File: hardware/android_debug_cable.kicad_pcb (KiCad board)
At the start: 2 copper layers, 36.7 x 12.2 mm, 12 parts, among them P1 USB_A, P2 CONN_01X04, P3 SJ-43514-SMT-TR, U1 TPS71718DCKR, U2 CP2103-GM

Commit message: Remove Copperhead branding, bump to v0.3
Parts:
- removed W1: LOGO, copperhead_logo:copperhead_logo
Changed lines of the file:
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@@
-(kicad_pcb (version 20160815) (host pcbnew 201610010949+7276~55~ubuntu16.04.1-)
+(kicad_pcb (version 20160815) (host pcbnew no-vcs-found-7409~56~ubuntu16.10.1)
   (general
     (links 33)
@@
     (tracks 205)
     (zones 0)
-    (modules 12)
+    (modules 11)
     (nets 10)
   )
@@
       (effects (font (size 0.7 0.7) (thickness 0.15)))
     )
-    (fp_text value SJ-43514-SMT-TR (at 3.8735 7.874 360) (layer F.Fab)
+    (fp_text value SJ-43514-SMT-TR (at 3.8735 7.874) (layer F.Fab)
       (effects (font (size 1 1) (thickness 0.15)))
     )
@@
     )
   )
-  (module copperhead_logo:copperhead_logo (layer B.Cu)
-    (at 94.2 82.1)
-    (fp_text reference W1 (at 0 0) (layer B.SilkS) hide
-      (effects (font (thickness 0.3)) (justify mirror))
-    )
-    (fp_text value LOGO (at 0.75 0) (layer B.SilkS) hide
-      (effects (font (thickness 0.3)) (justify mirror))
-    )
-    (fp_poly (pts (xy 0.286595 4.997953) (xy 0.652425 4.97361) (xy 0.978773 4.925874) (xy 1.513452 4.793043)
-      (xy 2.009899 4.611833) (xy 2.473986 4.379106) (xy 2.911581 4.091724) (xy 3.328554 3.746551)
-      (xy 3.50953 3.573031) (xy 3.882533 3.161764) (xy 4.196417 2.731413) (xy 4.45407 2.276573)
-      (xy 4.658382 1.791838) (xy 4.812242 1.271805) (xy 4.862373 1.042274) (xy 4.910585 0.711301)
-      (xy 4.934611 0.345163) (xy 4.934452 -0.032595) (xy 4.910109 -0.398425) (xy 4.862373 -0.724773)
-      (xy 4.728781 -1.261192) (xy 4.545946 -1.760049) (xy 4.31098 -2.226749) (xy 4.020993 -2.666697)
-      (xy 3.673096 -3.085297) (xy 3.50953 -3.25553) (xy 3.095062 -3.631) (xy 2.660805 -3.947073)
-      (xy 2.202899 -4.205819) (xy 1.717484 -4.409311) (xy 1.200701 -4.559619) (xy 1.000125 -4.602293)
-      (xy 0.77577 -4.637061) (xy 0.517751 -4.663239) (xy 0.246379 -4.679854) (xy -0.018034 -4.685937)
-      (xy -0.255177 -4.680517) (xy -0.396875 -4.669035) (xy -0.95683 -4.57297) (xy -1.492599 -4.418811)
-      (xy -2.001529 -4.208039) (xy -2.480971 -3.942137) (xy -2.928275 -3.622585) (xy -3.340789 -3.250867)
-      (xy -3.715863 -2.828462) (xy -3.736754 -2.802004) (xy -4.045523 -2.358026) (xy -4.29936 -1.886324)
-      (xy -4.497617 -1.392117) (xy -4.639646 -0.880626) (xy -4.724799 -0.357072) (xy -4.75243 0.173326)
-      (xy -4.722283 0.6985) (xy -2.604785 0.6985) (xy -2.51683 0.545361) (xy -2.30908 0.183999)
-      (xy -2.100804 -0.177609) (xy -1.894435 -0.535281) (xy -1.692406 -0.884836) (xy -1.497151 -1.222092)
-      (xy -1.311103 -1.542868) (xy -1.136697 -1.84298) (xy -0.976364 -2.118249) (xy -0.832538 -2.364491)
-      (xy -0.707654 -2.577526) (xy -0.604144 -2.753172) (xy -0.524441 -2.887246) (xy -0.47098 -2.975568)
-      (xy -0.446194 -3.013955) (xy -0.444822 -3.015284) (xy -0.426146 -2.988446) (xy -0.379172 -2.912028)
-      (xy -0.307152 -2.791559) (xy -0.213336 -2.632567) (xy -0.100976 -2.440581) (xy 0.026679 -2.221131)
-      (xy 0.166376 -1.979743) (xy 0.278627 -1.784971) (xy 0.442484 -1.500212) (xy 0.610981 -1.207497)
-      (xy 0.778367 -0.916808) (xy 0.93889 -0.63813) (xy 1.086799 -0.381446) (xy 1.216344 -0.15674)
-      (xy 1.321774 0.026006) (xy 1.348733 0.072699) (xy 1.711587 0.701022) (xy 1.454789 0.691824)
-      (xy 1.197992 0.682625) (xy 0.386323 -0.722312) (xy 0.228568 -0.994639) (xy 0.080067 -1.249569)
-      (xy -0.056115 -1.48194) (xy -0.176914 -1.686592) (xy -0.279267 -1.858364) (xy -0.36011 -1.992097)
-      (xy -0.416379 -2.082629) (xy -0.445011 -2.1248) (xy -0.447752 -2.12725) (xy -0.46749 -2.100571)
-      (xy -0.515783 -2.023965) (xy -0.589579 -1.902579) (xy -0.685822 -1.74156) (xy -0.80146 -1.546054)
-      (xy -0.933438 -1.321209) (xy -1.078703 -1.072172) (xy -1.234201 -0.804088) (xy -1.286053 -0.714375)
-      (xy -2.101947 0.6985) (xy -2.604785 0.6985) (xy -4.722283 0.6985) (xy -4.72189 0.705345)
-      (xy -4.632532 1.233766) (xy -4.483708 1.753369) (xy -4.345514 2.105153) (xy -4.127076 2.54)
-      (xy -2.597748 2.54) (xy -1.529062 0.6855) (xy -1.30419 0.296075) (xy -1.108823 -0.040466)
-      (xy -0.94143 -0.326643) (xy -0.800483 -0.564974) (xy -0.684453 -0.757975) (xy -0.59181 -0.908165)
-      (xy -0.521027 -1.018062) (xy -0.470574 -1.090183) (xy -0.438921 -1.127047) (xy -0.425271 -1.132188)
-      (xy -0.391849 -1.086032) (xy -0.340594 -1.003433) (xy -0.293013 -0.92075) (xy -0.19586 -0.746125)
-      (xy -1.01868 0.677698) (xy -1.177131 0.95212) (xy -1.325549 1.209622) (xy -1.460973 1.445034)
-      (xy -1.554371 1.607766) (xy -0.974568 1.607766) (xy -0.965463 1.57683) (xy -0.930335 1.506465)
-      (xy -0.876531 1.411264) (xy -0.870541 1.401166) (xy -0.754579 1.2065) (xy 0.896107 1.2065)
-      (xy 1.262239 1.206405) (xy 1.569856 1.206007) (xy 1.823946 1.205134) (xy 2.029492 1.203618)
-      (xy 2.191481 1.201289) (xy 2.3149 1.197976) (xy 2.404732 1.19351) (xy 2.465965 1.18772)
-      (xy 2.503583 1.180437) (xy 2.522573 1.17149) (xy 2.527921 1.16071) (xy 2.525835 1.150938)
-      (xy 2.506213 1.113162) (xy 2.457891 1.025927) (xy 2.383998 0.894724) (xy 2.28766 0.725043)
-      (xy 2.172005 0.522374) (xy 2.04016 0.292208) (xy 1.895252 0.040035) (xy 1.740408 -0.228655)
-      (xy 1.712813 -0.27646) (xy 1.557397 -0.546069) (xy 1.412076 -0.798995) (xy 1.279873 -1.029923)
-      (xy 1.163808 -1.233536) (xy 1.066903 -1.404515) (xy 0.992178 -1.537546) (xy 0.942656 -1.627309)
-      (xy 0.921357 -1.668489) (xy 0.92075 -1.670409) (xy 0.935226 -1.712536) (xy 0.972357 -1.786109)
-      (xy 1.022697 -1.875322) (xy 1.076798 -1.964366) (xy 1.125213 -2.037434) (xy 1.158496 -2.078718)
-      (xy 1.166855 -2.082227) (xy 1.185409 -2.052333) (xy 1.23301 -1.97199) (xy 1.307 -1.845768)
-      (xy 1.404723 -1.678237) (xy 1.523522 -1.473969) (xy 1.66074 -1.237534) (xy 1.813721 -0.973501)
-      (xy 1.979808 -0.686443) (xy 2.156345 -0.380929) (xy 2.24325 -0.230393) (xy 3.301579 1.603375)
-      (xy 1.169473 1.611538) (xy 0.80752 1.61275) (xy 0.464566 1.613561) (xy 0.145837 1.613981)
-      (xy -0.143443 1.614018) (xy -0.398046 1.613682) (xy -0.612748 1.612982) (xy -0.782322 1.611927)
-      (xy -0.901542 1.610527) (xy -0.965183 1.60879) (xy -0.974568 1.607766) (xy -1.554371 1.607766)
-      (xy -1.58044 1.653186) (xy -1.680989 1.828906) (xy -1.759658 1.967026) (xy -1.813485 2.062373)
-      (xy -1.839508 2.109778) (xy -1.8415 2.114102) (xy -1.810731 2.116667) (xy -1.722347 2.119366)
-      (xy -1.582232 2.122126) (xy -1.396271 2.124871) (xy -1.170348 2.127529) (xy -0.910348 2.130026)
-      (xy -0.622155 2.132287) (xy -0.311654 2.134239) (xy -0.184798 2.134905) (xy 1.471905 2.143125)
-      (xy 1.576091 2.31775) (xy 1.630232 2.41166) (xy 1.668352 2.483805) (xy 1.681513 2.516188)
-      (xy 1.65084 2.520218) (xy 1.561839 2.524034) (xy 1.419685 2.527578) (xy 1.229552 2.530792)
-      (xy 0.996611 2.533618) (xy 0.726038 2.536) (xy 0.423004 2.537879) (xy 0.092683 2.539198)
-      (xy -0.259752 2.539899) (xy -0.457499 2.54) (xy -2.597748 2.54) (xy -4.127076 2.54)
-      (xy -4.125196 2.543742) (xy -3.859523 2.954886) (xy -3.541054 3.349523) (xy -3.383147 3.519858)
-      (xy -2.974596 3.900625) (xy -2.535891 4.225754) (xy -2.065994 4.495807) (xy -1.563866 4.711348)
-      (xy -1.02847 4.872938) (xy -0.788274 4.925874) (xy -0.457301 4.974086) (xy -0.091163 4.998112)
-      (xy 0.286595 4.997953)) (layer B.SilkS) (width 0.01))
-  )
   (module Resistors_SMD:R_0402 (layer F.Cu)

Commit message: Add first version of v0.4
Signed-off-by: Robert Foss <robert.foss@collabora.com>
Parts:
- removed C5: 1uF, Capacitors_SMD:C_0402
- removed C6: 0.1uF, Capacitors_SMD:C_0402
- added C3: 1uF, Capacitors_SMD:C_0402, F.Cu at (138.8, 91.7)
- added G***: LOGO, memcpy_logo:memcpy_logo_13.2x3.6mm, B.Cu at (139.6, 88.8)
- C1: value 0.1uF -> 1uF
- P1: value USB_A -> USB_OTG; footprint connectors:usb-PCB -> Connectors:USB_Micro-B
- P2: value CONN_01X04 -> 50-00397; footprint footprints:CONN_2.54mm_1x4_no-outline -> 50-00397:50-00397
- P3: value SJ-43514-SMT-TR -> CONN_01X04; footprint 3-5mm_4pole_jack:3.5mm_4pin_jack -> footprints:CONN_2.54mm_1x4_no-outline
- R1: value 10k -> 1k
- U1: value TPS71718DCKR -> TCR2EF18; footprint TO_SOT_Packages_SMD:SC-70-5 -> TO_SOT_Packages_SMD:SOT-23-5
- U2: value CP2103-GM -> CP2102N-A01-GQFN24; footprint Housings_DFN_QFN:QFN-28-1EP_5x5mm_Pitch0.5mm -> Housings_DFN_QFN:QFN-24-1EP_4x4mm_Pitch0.5mm
- moved P1 57.3 mm to (135.2, 88.6)
- moved P2 55.9 mm to (157.9, 86.5), turned to 0 degrees
- moved R1 55.9 mm to (148.0, 89.9)
- moved U2 51.0 mm to (144.4, 87.4)
- moved C2 47.0 mm to (138.8, 90.6), turned to 0 degrees
- moved C1 46.7 mm to (138.8, 85.5), turned to 0 degrees
- moved U1 40.4 mm to (144.3, 92.0), turned to 180 degrees
- moved C4 37.9 mm to (138.8, 92.9), turned to 180 degrees
- moved P3 37.2 mm to (151.4, 84.9), turned to 0 degrees
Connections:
- C1 pad 1: GND -> Net-(C1-Pad1)
- C2 pad 1: GND -> Net-(C2-Pad1)
- C4 pad 1: V1.8 -> VCC
- P1 pad 4: GND -> (no net)
- P2 pad 1: RX -> V3.3
- P2 pad 3: GND -> RX
- P2 pad 4: V3.3 -> GND
- P3 pad 1: V3.3 -> RX
- P3 pad 3: RX -> GND
- P3 pad 4: GND -> V3.3
- R1 pad 1: VCC -> Net-(R1-Pad1)
- R1 pad 2: Net-(R1-Pad2) -> V1.8
- U2 pad 20: (no net) -> TX
- U2 pad 21: (no net) -> RX
- U2 pad 24: TX -> (no net)
- U2 pad 25: RX -> GND
- U2 pad 6: V3.3 -> Net-(C1-Pad1)
- U2 pad 7: VCC -> Net-(C2-Pad1)
- U2 pad 9: Net-(R1-Pad2) -> Net-(R1-Pad1)
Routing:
- net VCC: track 56.6 -> 35.1 mm
- net V3.3: track 42.0 -> 23.9 mm, vias 5 -> 2
- net GND: track 73.9 -> 88.7 mm, vias 1 -> 3
- net Net-(R1-Pad2): track 14.8 -> 0.00 mm
- net TX: track 17.1 -> 31.1 mm, vias 1 -> 6
- net Net-(C1-Pad1): track 0.00 -> 7.94 mm, vias 0 -> 2
- net RX: track 42.2 -> 36.1 mm
- net Net-(C2-Pad1): track 0.00 -> 5.38 mm
- net Net-(R1-Pad1): track 0.00 -> 4.39 mm
- net USB_D-: track 9.63 -> 6.01 mm
- net V1.8: track 25.3 -> 23.6 mm, vias 2 -> 5
- net USB_D+: track 8.76 -> 9.10 mm, vias 0 -> 2
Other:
- board size 36.7 x 12.2 mm -> 25.5 x 10.5 mm
- board text added: "v0.4"
- board text removed: "1.8V"
- board text removed: "Android Debug Cable v0.2"
- board text removed: "USB to UART VCC 3.3V VIO"

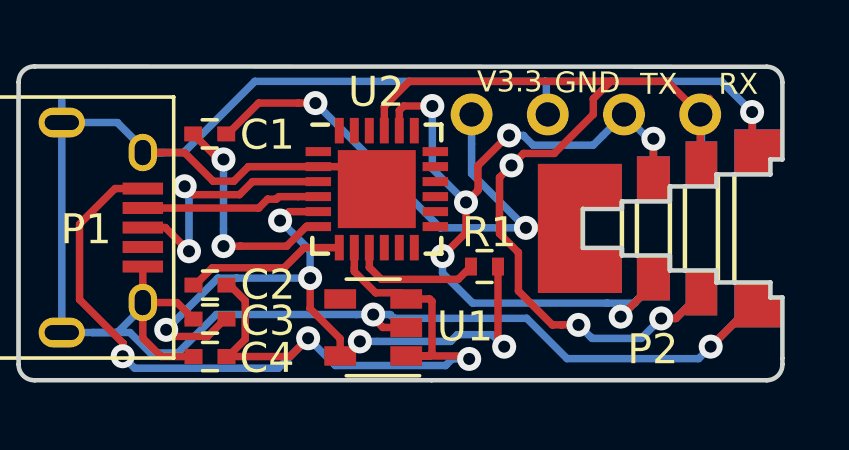
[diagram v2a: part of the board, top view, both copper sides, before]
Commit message: Changed 3.5mm connector pinout
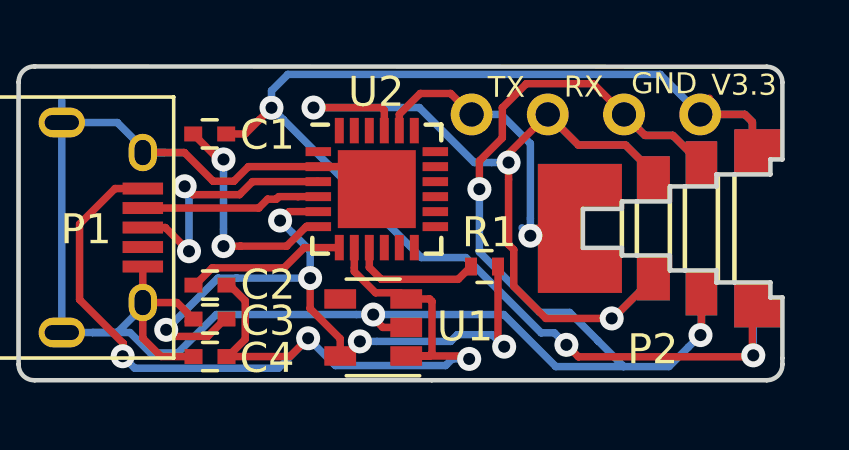
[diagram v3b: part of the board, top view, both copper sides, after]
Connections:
- P2 pad 1: V3.3 -> TX
- P2 pad 2: TX -> RX
- P2 pad 3: RX -> GND
- P2 pad 4: GND -> V3.3
- P3 pad 1: RX -> V3.3
- P3 pad 2: TX -> GND
- P3 pad 3: GND -> RX
- P3 pad 4: V3.3 -> TX
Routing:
- net V3.3: track 23.9 -> 50.4 mm, vias 2 -> 3
- net TX: track 31.1 -> 16.7 mm, vias 6 -> 1
- net GND: track 88.7 -> 84.4 mm
- net RX: track 36.1 -> 33.7 mm

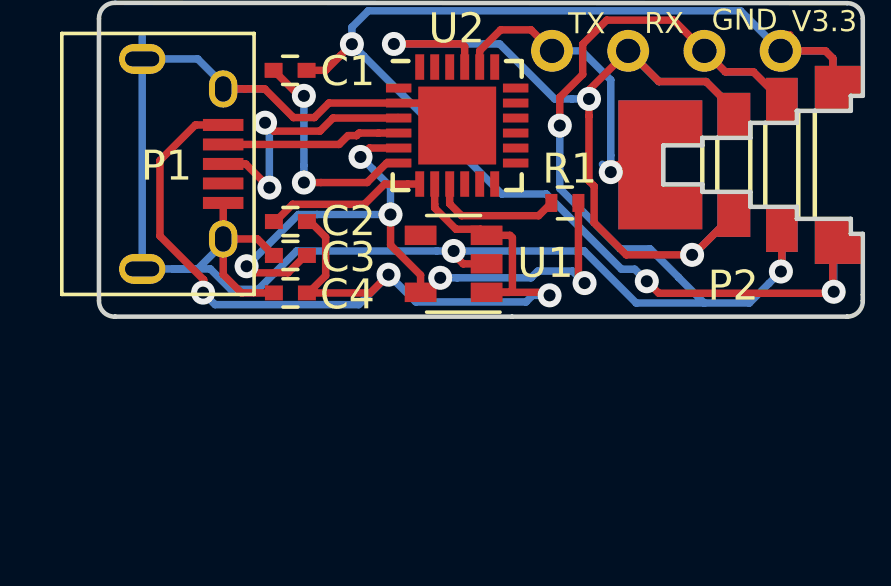
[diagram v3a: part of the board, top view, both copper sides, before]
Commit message: Fixed CP2102N power sourcing
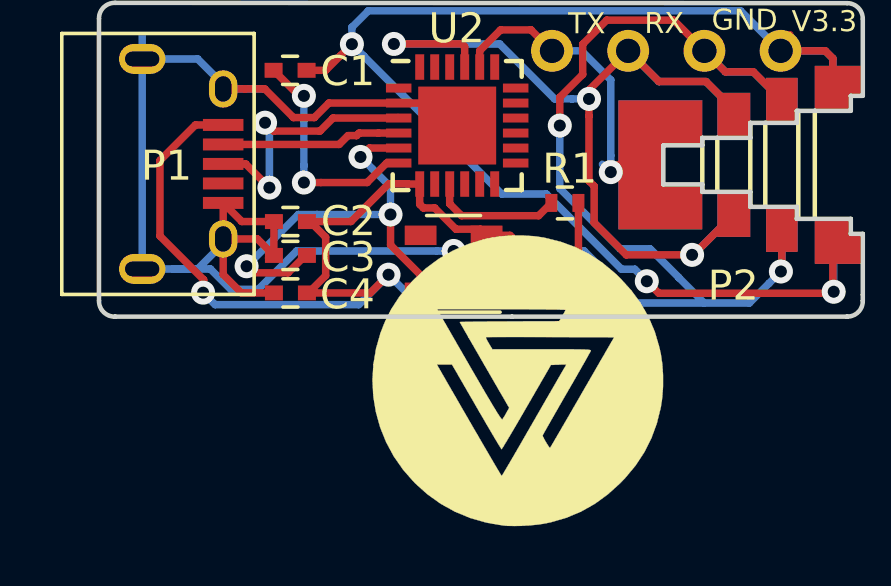
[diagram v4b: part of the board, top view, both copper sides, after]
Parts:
- added W1: LOGO, copperhead_logo:copperhead_logo, F.Cu at (146.3, 96.0)
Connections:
- C2 pad 1: Net-(C2-Pad1) -> GND
- U2 pad 7: Net-(C2-Pad1) -> VCC
- U2 pad 8: VCC -> (no net)
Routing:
- net Net-(C2-Pad1): track 5.38 -> 0.00 mm
- net VCC: track 35.1 -> 39.8 mm
- net GND: track 84.4 -> 87.5 mm

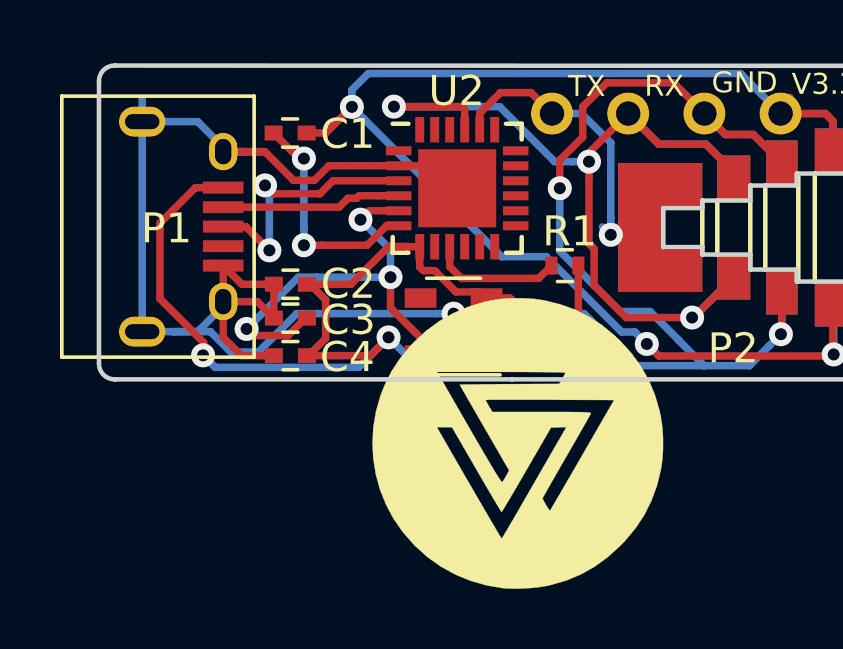
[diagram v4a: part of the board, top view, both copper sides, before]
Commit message: Edit MicoUSB footprint
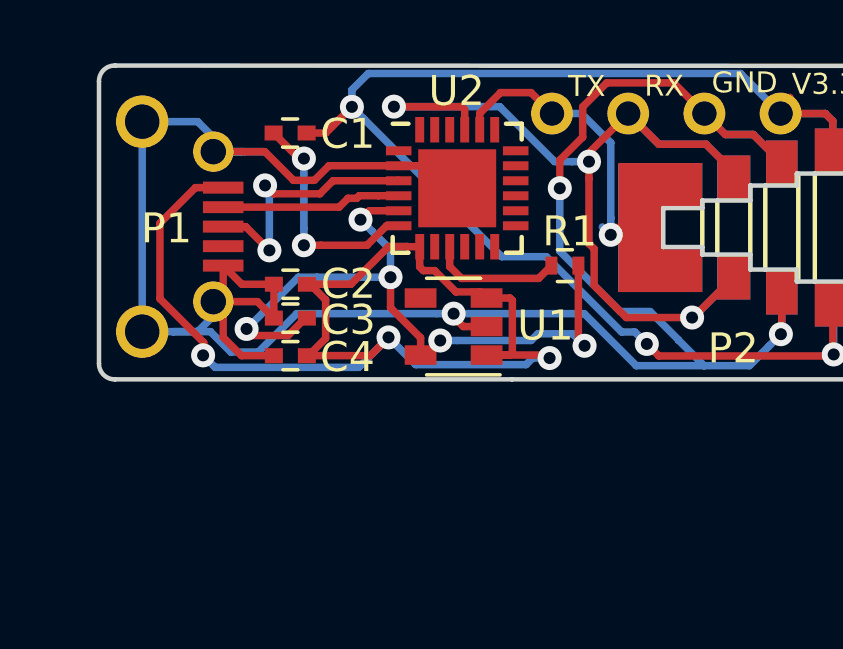
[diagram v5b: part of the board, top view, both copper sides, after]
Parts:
- removed W1: LOGO, copperhead_logo:copperhead_logo
- P1: footprint Connectors:USB_Micro-B -> usb_otg:USB_Micro-B

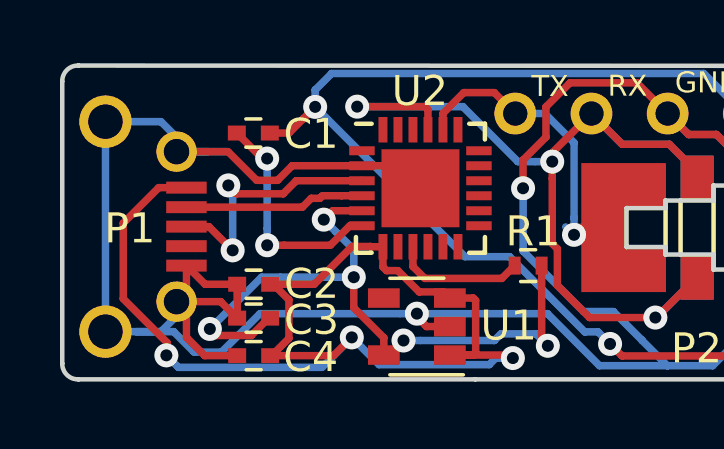
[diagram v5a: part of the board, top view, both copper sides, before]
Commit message: Move vias away from logo
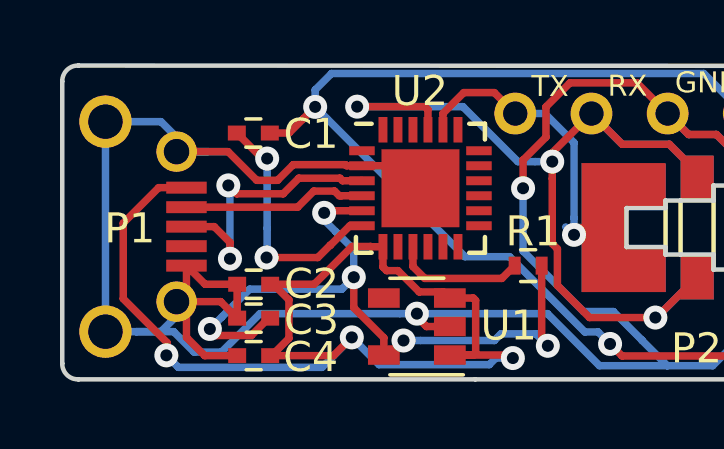
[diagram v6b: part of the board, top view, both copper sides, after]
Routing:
- net USB_D+: track 9.10 -> 9.83 mm

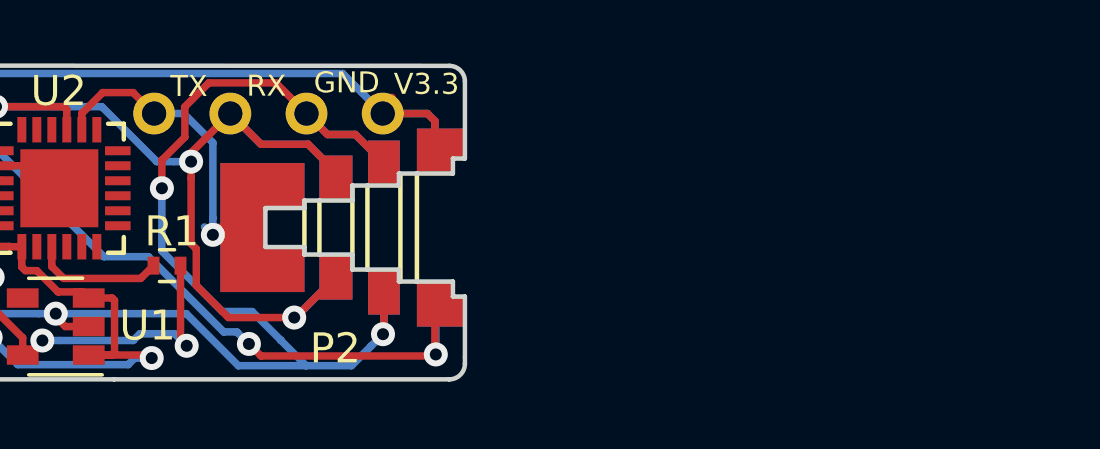
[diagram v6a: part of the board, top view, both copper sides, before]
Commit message: Add v0.5 using throughole 3.5mm connector
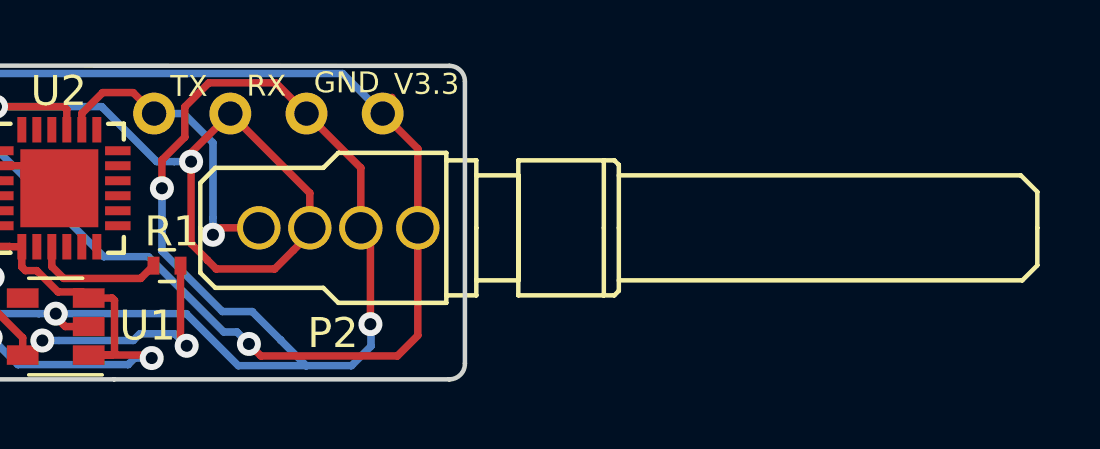
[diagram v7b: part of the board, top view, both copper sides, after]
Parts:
- P2: footprint 50-00397:50-00397 -> 54-00035:54-00035
- moved P2 9.09 mm to (149.1, 88.7)
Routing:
- net RX: track 33.7 -> 25.2 mm, vias 3 -> 2
- net TX: track 16.7 -> 11.1 mm
- net V3.3: track 50.4 -> 46.4 mm, vias 3 -> 2
- net GND: track 87.2 -> 85.5 mm
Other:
- outline, holes or cut-outs redrawn
- board text added: "v0.5"
- board text removed: "v0.4"
